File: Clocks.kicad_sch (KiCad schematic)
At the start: 9 parts, among them U3 CDCLVC1106, Y2 O 16,0-JT22CT-A-P-3,3-LF

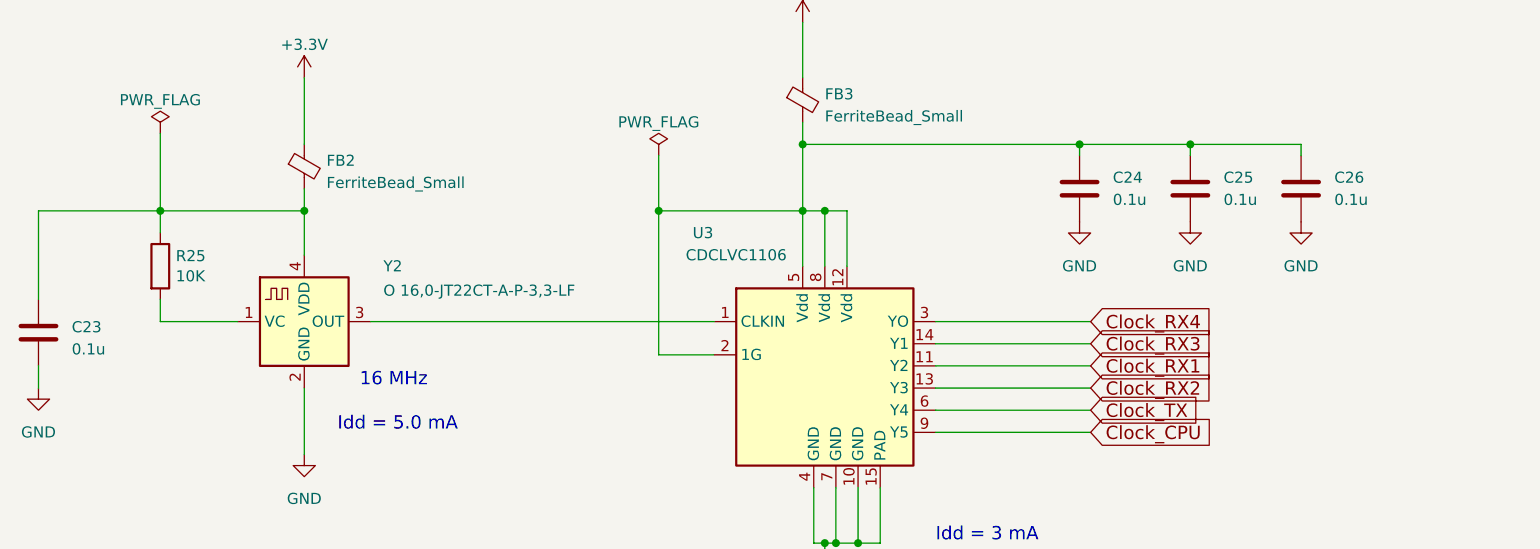
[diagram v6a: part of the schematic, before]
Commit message: Fix values of a lot of parts
Make them standard, 4.1p instead of 4p1, etc.

Add a tag to a couple of ICs that didn't have a pin 1 indicator on the
board.

Signed-off-by: Corey Minyard <corey@minyard.net>
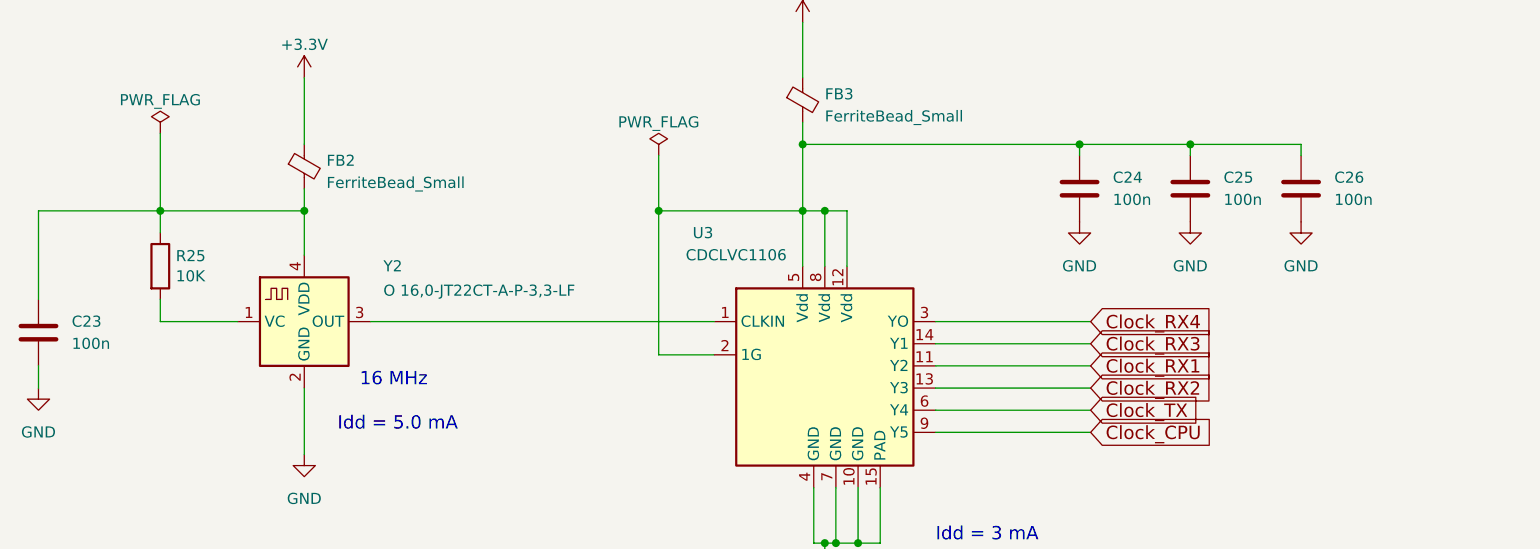
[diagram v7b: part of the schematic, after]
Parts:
- C23, C24, C25, C26: value 0.1u -> 100n
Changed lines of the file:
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@@
 			)
 		)
-		(property "Value" "0.1u"
+		(property "Value" "100n"
 			(at 248.92 92.7099 0)
 			(effects
@@
 		(fields_autoplaced yes)
 		(property "Reference" "C23"
-			(at 129.54 107.315 0)
+			(at 129.54 106.6799 0)
 			(effects
 				(font
@@
 			)
 		)
-		(property "Value" "0.1u"
-			(at 129.54 109.855 0)
+		(property "Value" "100n"
+			(at 129.54 109.2199 0)
 			(effects
 				(font
@@
 			)
 		)
-		(property "Value" "0.1u"
+		(property "Value" "100n"
 			(at 261.62 92.7099 0)
 			(effects
@@
 			)
 		)
-		(property "Value" "0.1u"
+		(property "Value" "100n"
 			(at 274.32 92.7099 0)
 			(effects

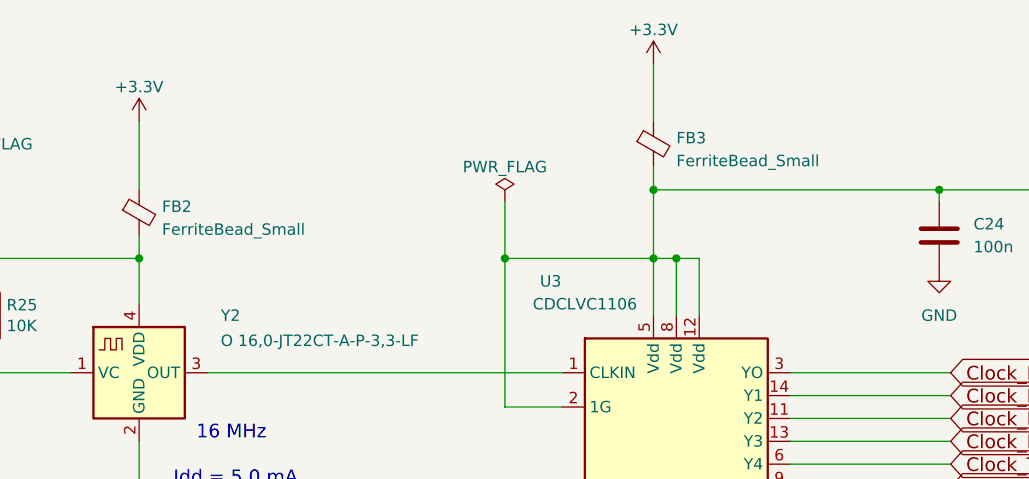
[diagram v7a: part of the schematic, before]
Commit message: Update ferrite beads with actual values
Signed-off-by: Corey Minyard <corey@minyard.net>
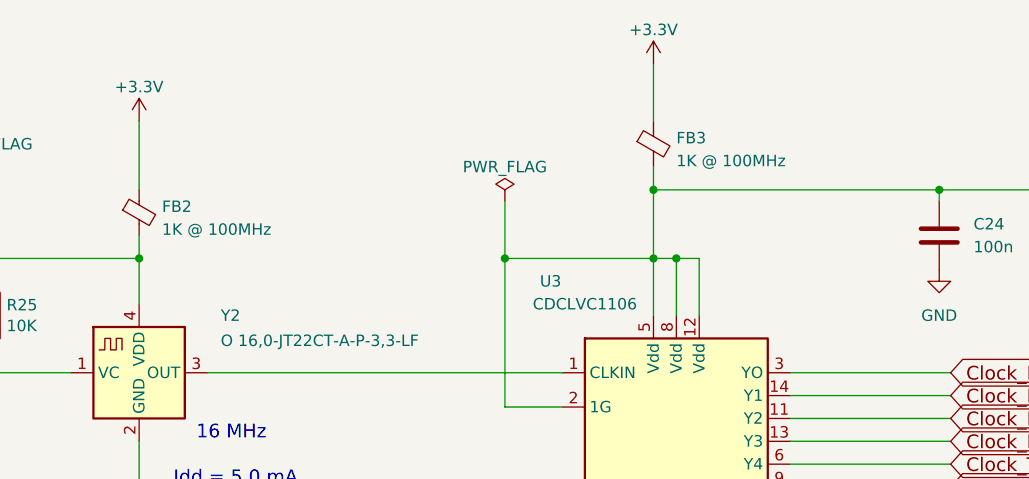
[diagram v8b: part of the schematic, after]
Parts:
- FB2, FB3: value FerriteBead_Small -> 1K @ 100MHz
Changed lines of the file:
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@@
 			)
 		)
-		(property "Value" "FerriteBead_Small"
+		(property "Value" "1K @ 100MHz"
 			(at 158.75 90.7669 0)
 			(effects
@@
 			)
 		)
-		(property "Description" ""
+		(property "Description" "FerriteBead_Small"
 			(at 156.21 88.9 0)
 			(effects
@@
 					(size 1.27 1.27)
 				)
+				(hide yes)
 			)
 		)
@@
 	)
 	(symbol
+		(lib_id "Device:C")
+		(at 125.73 107.95 0)
+		(unit 1)
+		(exclude_from_sim no)
+		(in_bom yes)
+		(on_board yes)
+		(dnp no)
+		(fields_autoplaced yes)
+		(property "Reference" "C23"
+			(at 129.54 106.6799 0)
+			(effects
+				(font
+					(size 1.27 1.27)
+				)
+				(justify left)
+			)
+		)
+		(property "Value" "100n"
+			(at 129.54 109.2199 0)
+			(effects
+				(font
+					(size 1.27 1.27)
+				)
+				(justify left)
+			)
+		)
+		(property "Footprint" "Capacitor_SMD:C_0603_1608Metric_Pad1.08x0.95mm_HandSolder"
+			(at 126.6952 111.76 0)
+			(effects
+				(font
+					(size 1.27 1.27)
+				)
+				(hide yes)
+			)
+		)
+		(property "Datasheet" "~"
+			(at 125.73 107.95 0)
+			(effects
+				(font
+					(size 1.27 1.27)
+				)
+				(hide yes)
+			)
+		)
+		(property "Description" ""
+			(at 125.73 107.95 0)
+			(effects
+				(font
+					(size 1.27 1.27)
+				)
+			)
+		)
+		(pin "1"
+		)
+		(pin "2"
+		)
+		(instances
+			(project "PacSat_Dev_RevD_240614"
+				(path "/cc9f42d2-6985-41ac-acab-5ab7b01c5b38/a735fef7-c3fa-4339-b3a6-fbce810c3c4b"
+					(reference "C23")
+					(unit 1)
+				)
+			)
+		)
+	)
+	(symbol
+		(lib_id "Oscillator:FT5HV")
+		(at 156.21 106.68 0)
+		(unit 1)
+		(exclude_from_sim no)
+		(in_bom yes)
+		(on_board yes)
+		(dnp no)
+		(property "Reference" "Y2"
+			(at 166.37 100.33 0)
+			(effects
+				(font
+					(size 1.27 1.27)
+				)
+			)
+		)
+		(property "Value" "O 16,0-JT22CT-A-P-3,3-LF"
+			(at 176.276 103.124 0)
+			(effects
+				(font
+					(size 1.27 1.27)
+				)
+			)
+		)
+		(property "Footprint" "Oscillator:Oscillator_SMD_SiT_PQFN-4Pin_2.5x2.0mm"
+			(at 156.21 125.73 0)
+			(effects
+				(font
+					(size 1.27 1.27)
+				)
+				(hide yes)
+			)
+		)
+		(property "Datasheet" ""
+			(at 156.21 106.68 0)
+			(effects
+				(font
+					(size 1.27 1.27)
+				)
+				(hide yes)
+			)
+		)
+		(property "Description" ""
+			(at 156.21 106.68 0)
+			(effects
+				(font
+					(size 1.27 1.27)
+				)
+			)
+		)
+		(pin "1"
+		)
+		(pin "2"
+		)
+		(pin "3"
+		)
+		(pin "4"
+		)
+		(instances
+			(project "PacSat_Dev_RevD_240614"
+				(path "/cc9f42d2-6985-41ac-acab-5ab7b01c5b38/a735fef7-c3fa-4339-b3a6-fbce810c3c4b"
+					(reference "Y2")
+					(unit 1)
+				)
+			)
+		)
+	)
+	(symbol
 		(lib_id "Device:FerriteBead_Small")
 		(at 213.36 81.28 0)
@@
 			)
 		)
-		(property "Value" "FerriteBead_Small"
+		(property "Value" "1K @ 100MHz"
 			(at 215.9 83.1469 0)
 			(effects
@@
 			)
 		)
-		(property "Description" ""
+		(property "Description" "FerriteBead_Small"
 			(at 213.36 81.28 0)
 			(effects
@@
 					(size 1.27 1.27)
 				)
+				(hide yes)
 			)
 		)
@@
 		)
 		(instances
-			(project "PacSat_Dev_RevD_240614"
+			(project "PacSat_AFSK"
 				(path "/cc9f42d2-6985-41ac-acab-5ab7b01c5b38/a735fef7-c3fa-4339-b3a6-fbce810c3c4b"
 					(reference "FB3")
 					(unit 1)
 				)
-			)
-		)
-	)
-	(symbol
-		(lib_id "Device:C")
-		(at 125.73 107.95 0)
-		(unit 1)
-		(exclude_from_sim no)
-		(in_bom yes)
-		(on_board yes)
-		(dnp no)
-		(fields_autoplaced yes)
-		(property "Reference" "C23"
-			(at 129.54 106.6799 0)
-			(effects
-				(font
-					(size 1.27 1.27)
-				)
-				(justify left)
-			)
-		)
-		(property "Value" "100n"
-			(at 129.54 109.2199 0)
-			(effects
-				(font
-					(size 1.27 1.27)
-				)
-				(justify left)
-			)
-		)
-		(property "Footprint" "Capacitor_SMD:C_0603_1608Metric_Pad1.08x0.95mm_HandSolder"
-			(at 126.6952 111.76 0)
-			(effects
-				(font
-					(size 1.27 1.27)
-				)
-				(hide yes)
-			)
-		)
-		(property "Datasheet" "~"
-			(at 125.73 107.95 0)
-			(effects
-				(font
-					(size 1.27 1.27)
-				)
-				(hide yes)
-			)
-		)
-		(property "Description" ""
-			(at 125.73 107.95 0)
-			(effects
-				(font
-					(size 1.27 1.27)
-				)
-			)
-		)
-		(pin "1"
-		)
-		(pin "2"
-		)
-		(instances
-			(project "PacSat_Dev_RevD_240614"
-				(path "/cc9f42d2-6985-41ac-acab-5ab7b01c5b38/a735fef7-c3fa-4339-b3a6-fbce810c3c4b"
-					(reference "C23")
-					(unit 1)
-				)
-			)
-		)
-	)
-	(symbol
-		(lib_id "Oscillator:FT5HV")
-		(at 156.21 106.68 0)
-		(unit 1)
-		(exclude_from_sim no)
-		(in_bom yes)
-		(on_board yes)
-		(dnp no)
-		(property "Reference" "Y2"
-			(at 166.37 100.33 0)
-			(effects
-				(font
-					(size 1.27 1.27)
-				)
-			)
-		)
-		(property "Value" "O 16,0-JT22CT-A-P-3,3-LF"
-			(at 176.276 103.124 0)
-			(effects
-				(font
-					(size 1.27 1.27)
-				)
-			)
-		)
-		(property "Footprint" "Oscillator:Oscillator_SMD_SiT_PQFN-4Pin_2.5x2.0mm"
-			(at 156.21 125.73 0)
-			(effects
-				(font
-					(size 1.27 1.27)
-				)
-				(hide yes)
-			)
-		)
-		(property "Datasheet" ""
-			(at 156.21 106.68 0)
-			(effects
-				(font
-					(size 1.27 1.27)
-				)
-				(hide yes)
-			)
-		)
-		(property "Description" ""
-			(at 156.21 106.68 0)
-			(effects
-				(font
-					(size 1.27 1.27)
-				)
-			)
-		)
-		(pin "1"
-		)
-		(pin "2"
-		)
-		(pin "3"
-		)
-		(pin "4"
-		)
-		(instances
-			(project "PacSat_Dev_RevD_240614"
-				(path "/cc9f42d2-6985-41ac-acab-5ab7b01c5b38/a735fef7-c3fa-4339-b3a6-fbce810c3c4b"
-					(reference "Y2")
-					(unit 1)
-				)
